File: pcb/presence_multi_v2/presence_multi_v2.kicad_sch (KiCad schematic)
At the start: 31 parts, among them IC1 LDL1117S33R, J1 USB_C_Receptacle_USB2.0_16P, J2 TC2050, J3 Conn_01x06_Socket, U3 CH340E, Y1 Wurth 830050789

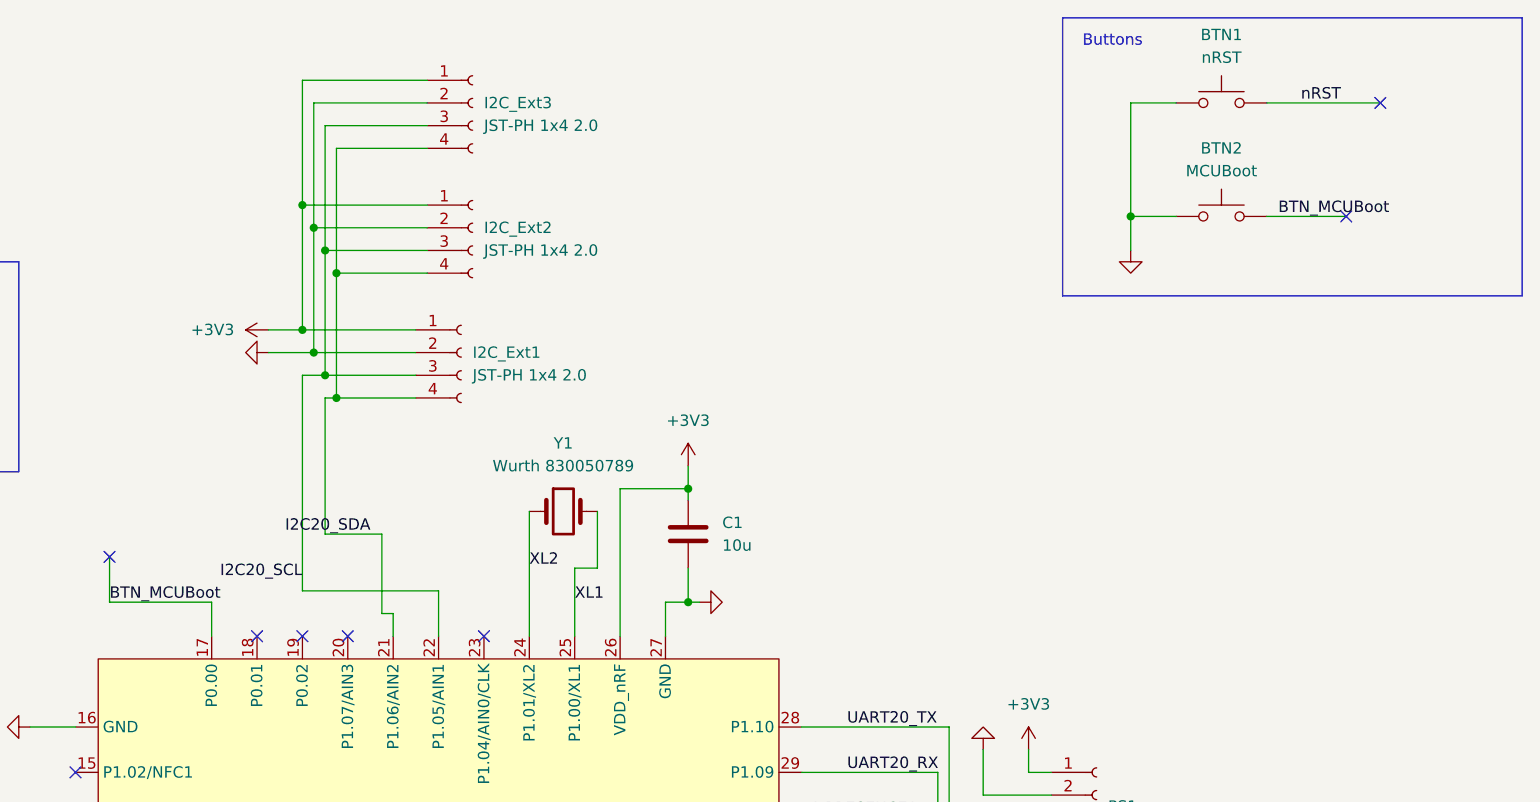
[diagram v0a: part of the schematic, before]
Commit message: added a dedicated button for zigbee
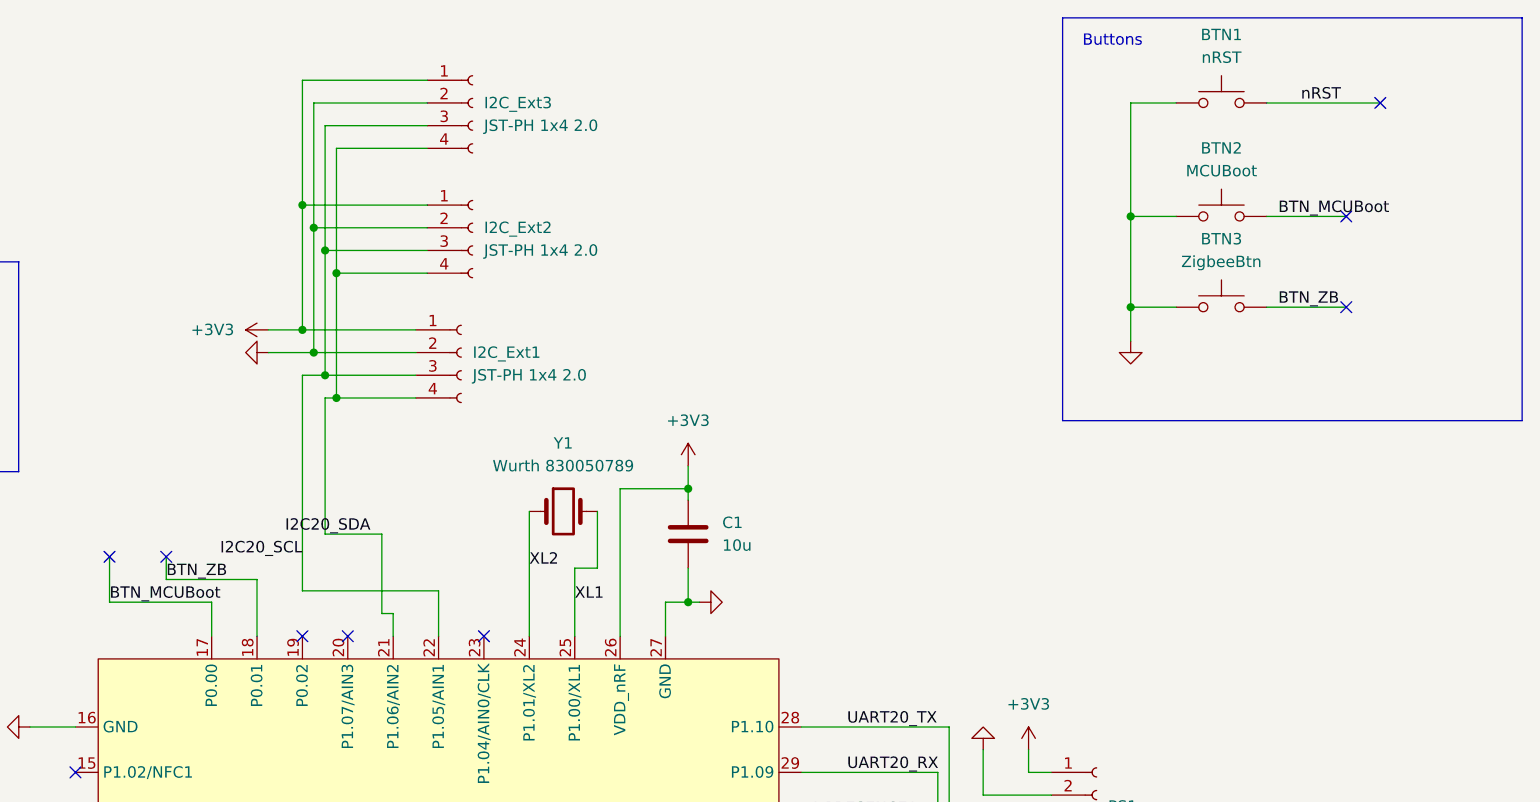
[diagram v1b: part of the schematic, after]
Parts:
- added BTN3: ZigbeeBtn, Button_Switch_SMD:SW_SPST_TS-1088-xR020, symbol Switch:SW_Push
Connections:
- net GND: now also BTN3.1
- net BTN_ZB: now reaches MCU1.18 (P0.01)
- net BTN_ZB: now also BTN3.2
- no-connect marks 22 -> 23
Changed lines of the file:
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@@
 	(rectangle
 		(start 306.07 26.035)
-		(end 357.505 57.15)
+		(end 357.505 71.12)
 		(stroke
 			(width 0)
@@
 	)
 	(junction
+		(at 313.69 58.42)
+		(diameter 0)
+		(color 0 0 0 0)
+	)
+	(junction
 		(at 97.79 62.23)
 		(diameter 0)
@@
 	)
 	(no_connect
+		(at 337.82 58.42)
+	)
+	(no_connect
 		(at 337.82 48.26)
 	)
@@
 	)
 	(no_connect
-		(at 215.9 95.25)
+		(at 163.83 149.86)
 	)
 	(no_connect
-		(at 163.83 149.86)
+		(at 205.74 86.36)
 	)
 	(wire
@@
 	(wire
 		(pts
+			(xy 205.74 86.36) (xy 205.74 88.9)
+		)
+		(stroke
+			(width 0)
+			(type default)
+		)
+	)
+	(wire
+		(pts
 			(xy 224.79 68.58) (xy 224.79 54.61)
 		)
@@
 	(wire
 		(pts
+			(xy 220.98 66.04) (xy 220.98 90.17)
+		)
+		(stroke
+			(width 0)
+			(type default)
+		)
+	)
+	(wire
+		(pts
 			(xy 328.93 48.26) (xy 337.82 48.26)
 		)
@@
 	(wire
 		(pts
+			(xy 313.69 58.42) (xy 318.77 58.42)
+		)
+		(stroke
+			(width 0)
+			(type default)
+		)
+	)
+	(wire
+		(pts
 			(xy 82.55 91.44) (xy 87.63 91.44)
 		)
@@
 	(wire
 		(pts
+			(xy 215.9 95.25) (xy 215.9 88.9)
+		)
+		(stroke
+			(width 0)
+			(type default)
+		)
+	)
+	(wire
+		(pts
 			(xy 82.55 86.36) (xy 82.55 88.9)
 		)
@@
 	(wire
 		(pts
-			(xy 220.98 66.04) (xy 220.98 90.17)
+			(xy 231.14 92.71) (xy 231.14 95.25)
 		)
 		(stroke
@@
 	(wire
 		(pts
-			(xy 231.14 92.71) (xy 231.14 95.25)
+			(xy 302.26 110.49) (xy 304.8 110.49)
 		)
 		(stroke
@@
 	(wire
 		(pts
-			(xy 302.26 110.49) (xy 304.8 110.49)
+			(xy 313.69 58.42) (xy 313.69 62.23)
 		)
 		(stroke
@@
 	(wire
 		(pts
+			(xy 215.9 88.9) (xy 205.74 88.9)
+		)
+		(stroke
+			(width 0)
+			(type default)
+		)
+	)
+	(wire
+		(pts
 			(xy 176.53 62.23) (xy 179.07 62.23)
 		)
@@
 	(wire
 		(pts
-			(xy 313.69 48.26) (xy 313.69 52.07)
+			(xy 313.69 48.26) (xy 313.69 58.42)
 		)
 		(stroke
@@
 	(wire
 		(pts
+			(xy 328.93 58.42) (xy 337.82 58.42)
+		)
+		(stroke
+			(width 0)
+			(type default)
+		)
+	)
+	(wire
+		(pts
 			(xy 220.98 33.02) (xy 234.95 33.02)
 		)
@@
 		)
 	)
+	(label "BTN_ZB"
+		(at 330.2 58.42 0)
+		(effects
+			(font
+				(size 1.27 1.27)
+			)
+			(justify left bottom)
+		)
+	)
 	(label "XL2"
 		(at 246.38 87.63 0)
@@
 	)
 	(label "I2C20_SCL"
-		(at 220.98 88.9 180)
+		(at 220.98 86.36 180)
 		(effects
 			(font
@@
 		)
 	)
+	(label "BTN_ZB"
+		(at 205.74 88.9 0)
+		(effects
+			(font
+				(size 1.27 1.27)
+			)
+			(justify left bottom)
+		)
+	)
 	(label "I_PRESENCE1"
 		(at 278.13 115.57 0)
@@
 	(symbol
 		(lib_id "power:GND")
-		(at 313.69 52.07 0)
+		(at 313.69 62.23 0)
 		(unit 1)
 		(exclude_from_sim no)
@@
 		(fields_autoplaced yes)
 		(property "Reference" "#PWR027"
-			(at 313.69 58.42 0)
+			(at 313.69 68.58 0)
 			(effects
 				(font
@@
 		)
 		(property "Value" "GND"
-			(at 313.6899 55.88 90)
+			(at 313.6899 66.04 90)
 			(effects
 				(font
@@
 		)
 		(property "Footprint" ""
-			(at 313.69 52.07 0)
+			(at 313.69 62.23 0)
 			(effects
 				(font
@@
 		)
 		(property "Datasheet" ""
-			(at 313.69 52.07 0)
+			(at 313.69 62.23 0)
 			(effects
 				(font
@@
 		)
 		(property "Description" "Power symbol creates a global label with name \"GND\" , ground"
-			(at 313.69 52.07 0)
+			(at 313.69 62.23 0)
 			(effects
 				(font
@@
 					(unit 1)
 				)
+			)
+		)
+	)
+	(symbol
+		(lib_id "Switch:SW_Push")
+		(at 323.85 58.42 0)
+		(unit 1)
+		(exclude_from_sim no)
+		(in_bom yes)
+		(on_board yes)
+		(dnp no)
+		(fields_autoplaced yes)
+		(property "Reference" "BTN3"
+			(at 323.85 50.8 0)
+			(effects
+				(font
+					(size 1.27 1.27)
+				)
+			)
+		)
+		(property "Value" "ZigbeeBtn"
+			(at 323.85 53.34 0)
+			(effects
+				(font
+					(size 1.27 1.27)
+				)
+			)
+		)
+		(property "Footprint" "Button_Switch_SMD:SW_SPST_TS-1088-xR020"
+			(at 323.85 53.34 0)
+			(effects
+				(font
+					(size 1.27 1.27)
+				)
+				(hide yes)
+			)
+		)
+		(property "Datasheet" "~"
+			(at 323.85 53.34 0)
+			(effects
+				(font
+					(size 1.27 1.27)
+				)
+				(hide yes)
+			)
+		)
+		(property "Description" "Push button switch, generic, two pins"
+			(at 323.85 58.42 0)
+			(effects
+				(font
+					(size 1.27 1.27)
+				)
+				(hide yes)
+			)
+		)
+		(pin "1"
+		)
+		(pin "2"
+		)
+		(instances
+			(project "presence_multi_v2"
+				(path "/c83d98d1-41ba-4e6e-b42b-963b3259de31"
+					(reference "BTN3")
+					(unit 1)
+				)

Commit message: ready version
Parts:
- Y1: footprint Crystal:Crystal_SMD_2012-2Pin_2.0x1.2mm -> theorlangur:Wurth-XTAL-830050789
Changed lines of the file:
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@@
 			)
 		)
-		(property "Footprint" "Crystal:Crystal_SMD_2012-2Pin_2.0x1.2mm"
+		(property "Footprint" "theorlangur:Wurth-XTAL-830050789"
 			(at 250.19 81.28 0)
 			(effects
